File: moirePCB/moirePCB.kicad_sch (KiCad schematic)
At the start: 28 parts, among them J1 USB_C_Receptacle, J2 Conn_01x12_Pin, SW1 SW_Push, SW3 SW_DPDT_x2, U1 ESP32-PICO-D4, U2 BQ24075RGT, U3 UA78M33, U4 RFM95W-915S2, U5 CH340E, Y2 32.768kHz

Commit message: New Pins
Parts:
- added CLK1: Conn_01x02_Pin, Connector_PinSocket_2.54mm:PinSocket_1x02_P2.54mm_Vertical, symbol Connector:Conn_01x02_Pin
- added GND1, VCC1: Conn_01x03_Pin, Connector_PinSocket_2.54mm:PinSocket_1x03_P2.54mm_Vertical, symbol Connector:Conn_01x03_Pin
- added ONOFF1: SW_DPDT_x2, Button_Switch_SMD:SW_SPDT_PCM12, symbol Switch:SW_DPDT_x2
- J2: footprint Connector_PinHeader_2.54mm:PinHeader_1x12_P2.54mm_Vertical -> Connector_PinSocket_2.54mm:PinSocket_1x12_P2.54mm_Vertical
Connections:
- net GND: now also GND1.1 (Pin_1), GND1.2 (Pin_2), GND1.3 (Pin_3), ONOFF1.1 (A); no longer U2.15 (SYSOFF)
- net GPIO_18: now also CLK1.1 (Pin_1), CLK1.2 (Pin_2)
- net VCC: now also VCC1.1 (Pin_1), VCC1.2 (Pin_2), VCC1.3 (Pin_3)
- new net: ONOFF1.2 (B), U2.15 (SYSOFF)

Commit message: sensor
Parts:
- added C1: 100n, Capacitor_SMD:C_0805_2012Metric, symbol Device:C
- added C2: 10n, Capacitor_SMD:C_0805_2012Metric, symbol Device:C
- added R1: 10k, Resistor_SMD:R_0805_2012Metric, symbol Device:R
- added R2: 1M, Resistor_SMD:R_0805_2012Metric, symbol Device:R
- added U1: TLC555xD, Package_SO:SOIC-8_3.9x4.9mm_P1.27mm, symbol Timer:TLC555xD
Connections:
- net GND: now also C1.2, C2.2, U1.1 (GND)
- net VCC: now also C1.1, R1.2, U1.4 (R), U1.8 (VCC)
- new net: R1.1, R2.1, U1.7 (DIS)
- new net: C2.1, U1.5 (CV)
- new net FREQOUT: U1.3 (Q)
- new net PROBE: R2.2, U1.2 (TR), U1.6 (THR)

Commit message: maddie call
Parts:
- removed R4: 10k, Resistor_SMD:R_0805_2012Metric, symbol Device:R
- removed R7: 4.7k, Resistor_SMD:R_0805_2012Metric, symbol Device:R
- removed U3: UA78M33, Package_TO_SOT_SMD:SOT-223-3_TabPin2, symbol Regulator_Linear:uA7805
- added SW2: SW_Push, Button_Switch_SMD:SW_Push_1P1T_XKB_TS-1187A, symbol Switch:SW_Push
- added U3: TLV73333PDBV, Package_TO_SOT_SMD:SOT-23-5, symbol Regulator_Linear:TLV73333PDBV
- added U7: HDC1080, Package_SON:Texas_PWSON-N6, symbol Sensor_Humidity:HDC1080
- AE1: footprint MountingHole:MountingHole_2.7mm_M2.5_DIN965_Pad_TopBottom -> Connector_PinHeader_2.54mm:PinHeader_1x01_P2.54mm_Vertical; LCSC Part # (none) -> C726086
- J1: footprint Connector_USB:USB_C_Receptacle_JAE_DX07S016JA1R1500 -> Connector_USB:USB_C_Receptacle_HRO_TYPE-C-31-M-12; LCSC Part # (none) -> C5329561
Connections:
- net FREQOUT: now also U1.15 (IO26)
- net GND: now also SW2.1, U3.2 (GND), U7.2 (GND)
- net GPIO_18: now also U7.6 (SCL)
- net GPIO_22: now also U7.1 (SDA); no longer J2.7 (Pin_7)
- net RX: now also U5.8 (TXD); no longer U5.9 (RXD)
- net TX: now also U5.9 (RXD); no longer U5.8 (TXD)
- net VCC: now also U3.5 (OUT), U7.5 (VCC)
- net at C3.2, CHG1.2 (A), PGOOD1.2 (A)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: now also U3.1 (IN), U3.3 (EN)
- net GPIO_26: no longer names the net of J2.9 (Pin_9)
- net GPIO_26: no longer U1.15 (IO26)
- net IO0: no longer names the net of U1.23 (IO0)
- net IO0: now also SW2.2; no longer U5.6 (TNOW)

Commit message: component updates
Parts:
- renumbered SW2 to BOOT1, SW1 to EN1
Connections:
- net GND: now also BOOT1.2; no longer BOOT1.1
- net at U1.23 (IO0): now also BOOT1.1; no longer BOOT1.2
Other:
- note added: "Soil Cond. Sensor"
- note added: "Temp/humidity Sensor"
- note added: "USB/UART Converter"
- moved on the sheet: BOOT1, C1, C2, EN1, J2, R1, R2, U1, U7

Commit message: layout changes
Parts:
- SC1: footprint Connector_PinHeader_2.54mm:PinHeader_1x02_P2.54mm_Vertical -> Connector_PinHeader_2.54mm:PinHeader_1x02_P2.54mm_Horizontal
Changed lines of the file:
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@@
       (effects (font (size 1.27 1.27)) (justify left))
     )
-    (property "Footprint" "Connector_PinHeader_2.54mm:PinHeader_1x02_P2.54mm_Vertical" (at 33.02 149.606 90)
+    (property "Footprint" "Connector_PinHeader_2.54mm:PinHeader_1x02_P2.54mm_Horizontal" (at 33.02 149.606 90)
       (effects (font (size 1.27 1.27)) hide)
     )

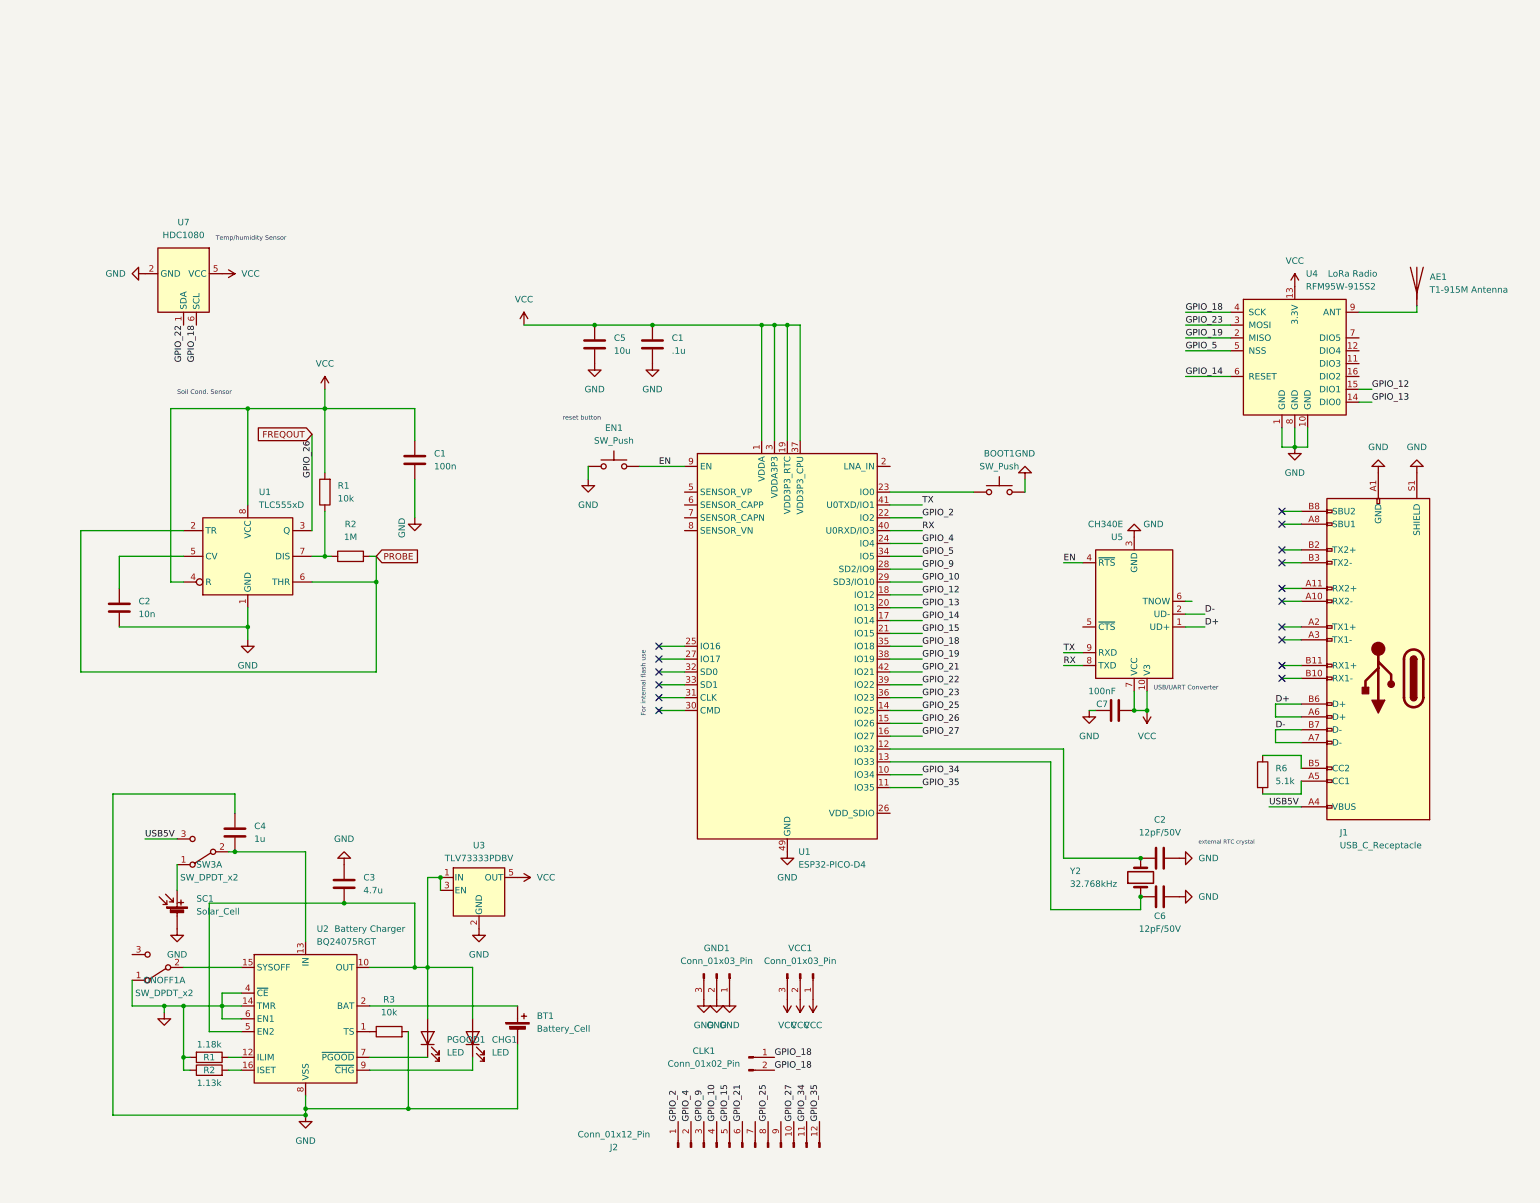
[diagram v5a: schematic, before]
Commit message: pins and jumpers, transistor A_RAIL
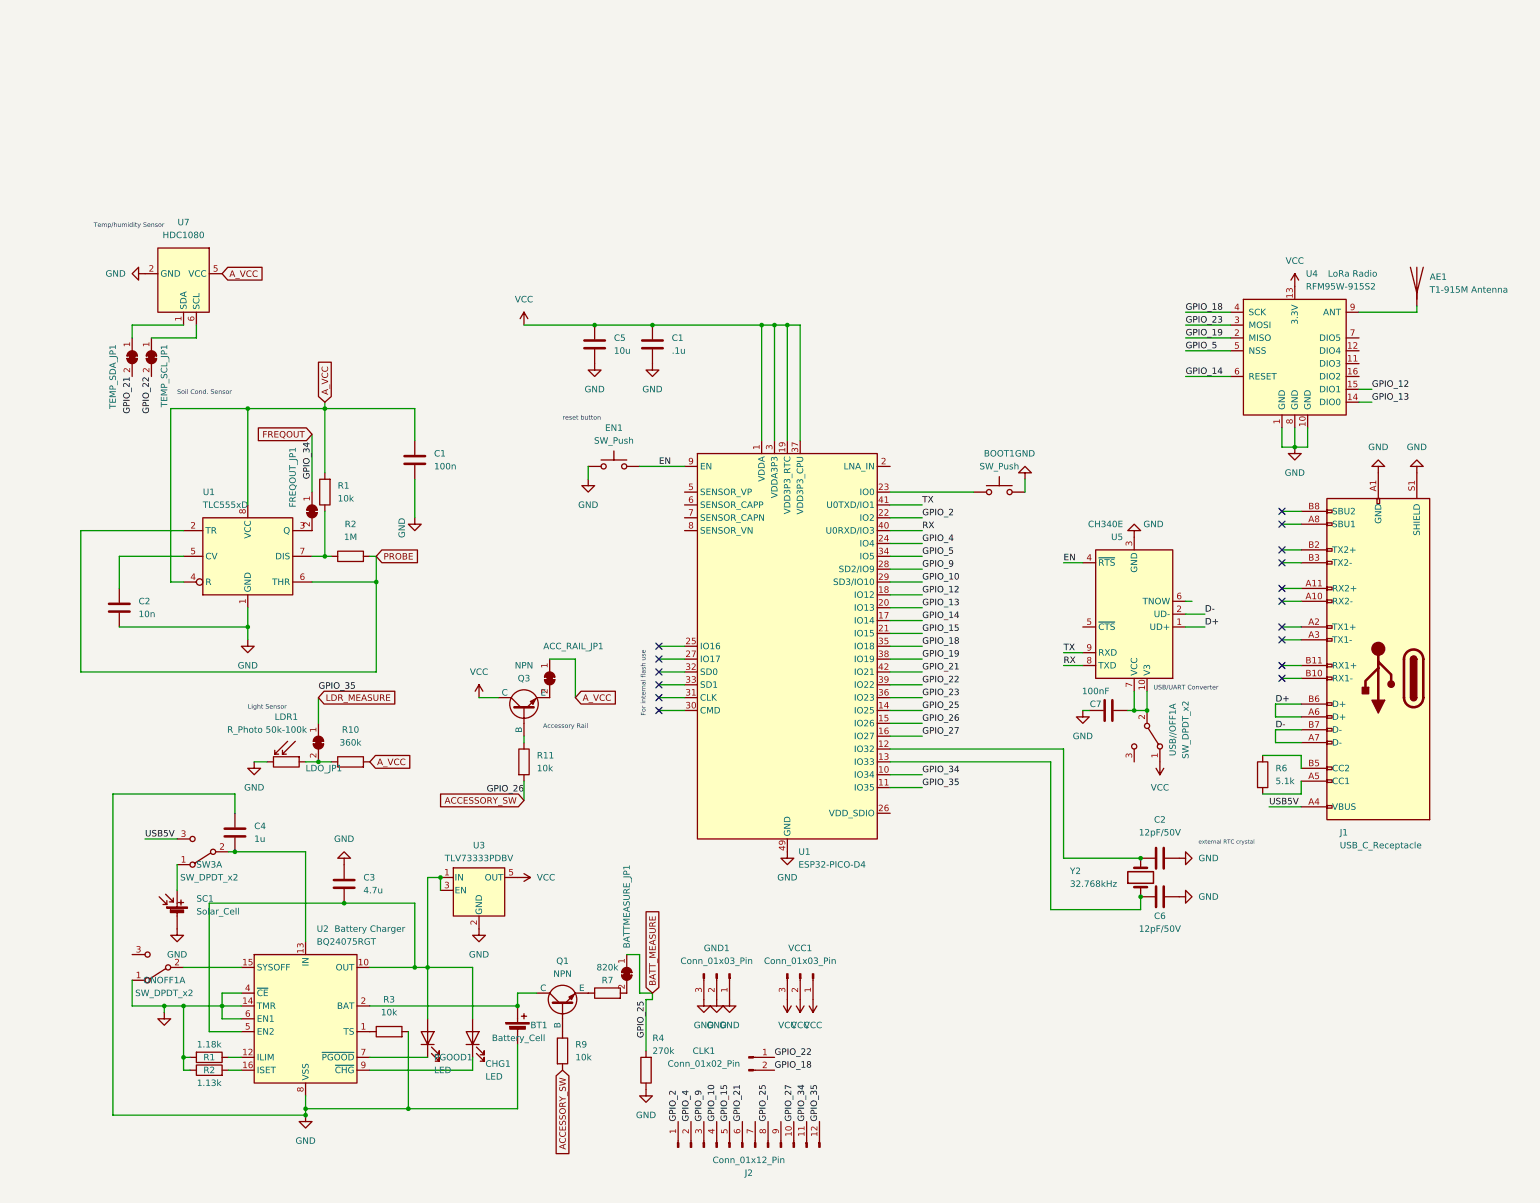
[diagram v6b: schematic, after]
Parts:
- added ACC_RAIL_JP1, BATTMEASURE_JP1, FREQOUT_JP1, LDO_JP1, TEMP_SCL_JP1, TEMP_SDA_JP1: SolderJumper_2_Bridged, Jumper:SolderJumper-2_P1.3mm_Bridged_RoundedPad1.0x1.5mm, symbol Jumper:SolderJumper_2_Bridged
- added LDR1: R_Photo 50k-100k, Connector_PinHeader_2.54mm:PinHeader_1x02_P2.54mm_Horizontal, symbol Device:R_Photo
- added Q1, Q3: NPN, Package_TO_SOT_SMD:TSOT-23, symbol Simulation_SPICE:NPN
- added R10: 360k, Resistor_SMD:R_0805_2012Metric, symbol Device:R
- added R11, R9: 10k, Resistor_SMD:R_0805_2012Metric, symbol Device:R
- added R4: 270k, Resistor_SMD:R_0805_2012Metric, symbol Device:R
- added R7: 820k, Resistor_SMD:R_0805_2012Metric, symbol Device:R
- added USB//OFF1: SW_DPDT_x2, Button_Switch_SMD:SW_SPDT_PCM12, symbol Switch:SW_DPDT_x2
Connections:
- net GPIO_34 is gone; now on net FREQOUT: J2.11 (Pin_11), U1.10 (IO34)
- net FREQOUT: now also FREQOUT_JP1.1 (A); no longer U1.15 (IO26), U1.3 (Q)
- net GND: now also LDR1.2, R4.1
- net GPIO_18: no longer CLK1.1 (Pin_1), U7.6 (SCL)
- net GPIO_21: now also TEMP_SDA_JP1.2 (B)
- net GPIO_22: now also CLK1.1 (Pin_1), TEMP_SCL_JP1.2 (B); no longer U7.1 (SDA)
- net VCC: now also Q3.1 (C), USB//OFF1.1 (A); no longer C1.1, C7.1, R1.2, U1.4 (R), U1.8 (VCC), U5.10 (V3), U5.7 (VCC), U7.5 (VCC)
- net at BT1.1 (+), U2.2 (BAT), U2.3 (BAT): now also Q1.1 (C)
- net GPIO_25 renamed BATT_MEASURE
- net BATT_MEASURE: now also BATTMEASURE_JP1.1 (A), R4.2
- new net: Q1.3 (E), R7.1
- new net: BATTMEASURE_JP1.2 (B), R7.2
- new net: C7.1, U5.10 (V3), U5.7 (VCC), USB//OFF1.2 (B)
- new net: LDO_JP1.2 (B), LDR1.1, R10.1
- new net: Q3.2 (B), R11.1
- new net: ACC_RAIL_JP1.2 (B), Q3.3 (E)
- new net: FREQOUT_JP1.2 (B), U1.3 (Q)
- new net: TEMP_SDA_JP1.1 (A), U7.1 (SDA)
- new net: TEMP_SCL_JP1.1 (A), U7.6 (SCL)
- new net: Q1.2 (B), R9.1
- new net ACCESSORY_SW: R11.2, R9.2, U1.15 (IO26)
- new net A_VCC: ACC_RAIL_JP1.1 (A), C1.1, R1.2, R10.2, U1.4 (R), U1.8 (VCC), U7.5 (VCC)
- new net LDR_MEASURE: LDO_JP1.1 (A)
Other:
- note added: "Accessory Rail"
- note added: "Light Sensor"
- moved on the sheet: C7

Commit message: pcb 2 final (submitted to jlc)
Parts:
- removed J2: Conn_01x12_Pin, Connector_PinSocket_2.54mm:PinSocket_1x12_P2.54mm_Vertical, symbol Connector:Conn_01x12_Pin
- removed Q1, Q3: NPN, Package_TO_SOT_SMD:TSOT-23, symbol Simulation_SPICE:NPN
- added EN2_JP1: SolderJumper_2_Bridged, Jumper:SolderJumper-2_P1.3mm_Bridged_RoundedPad1.0x1.5mm, symbol Jumper:SolderJumper_2_Bridged
- added J2: Conn_01x06_Socket, Connector_PinSocket_2.54mm:PinSocket_1x06_P2.54mm_Vertical, symbol Connector:Conn_01x06_Socket
- added U8, U9: AP2281-1WG-7, Package_TO_SOT_SMD:SOT-23-6, symbol Power_Management:AP2281-1WG-7
- R1: value 1.18k -> 7.5k
- R11, R9: value 10k -> 1k
- R2: value 1.13k -> 8.2
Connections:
- net GPIO_35 is gone; now on net LDR_MEASURE: U1.11 (IO35)
- net VCC is gone; now on net IN: C1.1, C5.1, U1.1 (VDDA), U1.19 (VDD3P3_RTC), U1.3 (VDDA3P3), U1.37 (VDD3P3_CPU), U1.4 (VDDA3P3), U1.43 (VDDA), U1.46 (VDDA), U3.5 (OUT), U4.13 (3.3V), USB//OFF1.1 (A), VCC1.1 (Pin_1), VCC1.2 (Pin_2), VCC1.3 (Pin_3)
- net ACCESSORY_SW: now also U8.3 (EN), U9.3 (EN); no longer R11.2, R9.2
- net GND: now also EN2_JP1.1 (A), U8.2 (GND), U8.5 (GND), U9.2 (GND), U9.5 (GND)
- net GPIO_10: now also J2.4 (Pin_4)
- net GPIO_15: now also J2.5 (Pin_5)
- net GPIO_2: now also J2.1 (Pin_1)
- net GPIO_27: now also J2.6 (Pin_6)
- net GPIO_4: now also J2.2 (Pin_2)
- net GPIO_9: now also J2.3 (Pin_3)
- net IN: now reaches BT1.1 (+), U2.2 (BAT), U2.3 (BAT)
- net IN: now also U8.4 (IN), U8.6 (IN), U9.4 (IN), U9.6 (IN)
- net at C3.2, U2.10 (OUT), U2.11 (OUT)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: now also R11.1, R9.1; no longer CHG1.2 (A), PGOOD1.2 (A), U2.5 (EN2)
- net at R7.1: now also U8.1 (OUT)
- net at ACC_RAIL_JP1.2 (B): now also U9.1 (OUT)
- new net: CHG1.2 (A), R9.2
- new net: EN2_JP1.2 (B), U2.5 (EN2)
- new net: PGOOD1.2 (A), R11.2
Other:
- moved on the sheet: ACC_RAIL_JP1, BATTMEASURE_JP1, CLK1, GND1, R4, R7, VCC1

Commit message: bq25504
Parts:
- removed C4: 1u, Capacitor_SMD:C_0805_2012Metric, symbol Device:C
- removed CHG1, PGOOD1: LED, LED_SMD:LED_0805_2012Metric, symbol Device:LED
- removed EN2_JP1: SolderJumper_2_Bridged, Jumper:SolderJumper-2_P1.3mm_Bridged_RoundedPad1.0x1.5mm, symbol Jumper:SolderJumper_2_Bridged
- removed ONOFF1, SW3: SW_DPDT_x2, Button_Switch_SMD:SW_SPDT_PCM12, symbol Switch:SW_DPDT_x2
- removed R1: 7.5k, Resistor_SMD:R_0805_2012Metric, symbol Device:R
- removed R11, R9: 1k, Resistor_SMD:R_0805_2012Metric, symbol Device:R
- removed R2: 8.2, Resistor_SMD:R_0805_2012Metric, symbol Device:R
- removed R3: 10k, Resistor_SMD:R_0805_2012Metric, symbol Device:R
- removed U2: BQ24075RGT, Package_DFN_QFN:VQFN-16-1EP_3x3mm_P0.5mm_EP1.6x1.6mm, symbol Battery_Management:BQ24075RGT
- added C_FLTR: .1uF, symbol Device:C
- added C_HVR, C_STOR: 4.7uF, symbol Device:C
- added L_BST: 22uH, symbol Device:L
- added R_OC_1, R_OC_2, R_OK_1, R_OK_2, R_OK_3, R_OV_1, R_OV_2, R_UV_1, R_UV_2: R, symbol Device:R
- added U10: TLV73333PDBV, Package_TO_SOT_SMD:SOT-23-5, symbol Regulator_Linear:TLV73333PDBV
- added U2: BQ25504, Package_DFN_QFN:VQFN-16-1EP_3x3mm_P0.5mm_EP1.68x1.68mm, symbol Battery_Management:BQ25504
- added USB//SOLAR: SW_DPDT_x2, Button_Switch_SMD:SW_SPDT_PCM12, symbol Switch:SW_DPDT_x2
- C3: value 4.7u -> .01uF; footprint Capacitor_SMD:C_0805_2012Metric -> (none)
- SC1: footprint Connector_PinHeader_2.54mm:PinHeader_1x02_P2.54mm_Horizontal -> (none)
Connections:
- net GND: now also C_FLTR.2, C_HVR.2, C_STOR.1, R_OC_1.1, R_OK_1.2, R_OV_1.1, R_UV_1.2, U10.2 (GND), U2.1 (VSS), U2.12 (AVSS), U2.13 (VSS), U2.17 (PAD), U2.5 (OT_PROG)
- net IN: now also U10.5 (OUT), U2.14 (VBAT); no longer U3.5 (OUT)
- net USB5V: now also U3.1 (IN), U3.3 (EN)
- net at SC1.1 (+): now also C_HVR.1, L_BST.1, USB//SOLAR.3 (C)
- new net: U3.5 (OUT), USB//SOLAR.1 (A)
- new net: R_OK_1.1, R_OK_2.1, U2.10 (OK_PROG)
- new net: C_FLTR.1, C_STOR.2, U10.1 (IN), U2.15 (VSTOR)
- new net: L_BST.2, U2.16 (LBST)
- new net: R_OC_2.1, U2.2 (VIN_DC), USB//SOLAR.2 (B)
- new net: R_OC_1.2, R_OC_2.2, U2.3 (VOC_SAMP)
- new net: C3.2, U2.4 (VREF_SAMP)
- new net: R_OV_1.2, R_OV_2.1, U2.6 (VBAT_OV)
- new net: R_OK_3.2, R_OV_2.2, R_UV_2.1, U2.7 (VRDIV)
- new net: R_UV_1.1, R_UV_2.2, U2.8 (VBAT_UV)
- new net: R_OK_2.2, R_OK_3.1, U2.9 (OK_HYST)
- new net VBAT_OK: U10.3 (EN), U2.11 (VBAT_OK)
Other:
- note added: "check this"
- moved on the sheet: LDO_JP1, LDR1, R10
